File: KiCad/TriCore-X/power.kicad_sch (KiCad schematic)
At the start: 13 parts, among them U3 TPS56637RPAR

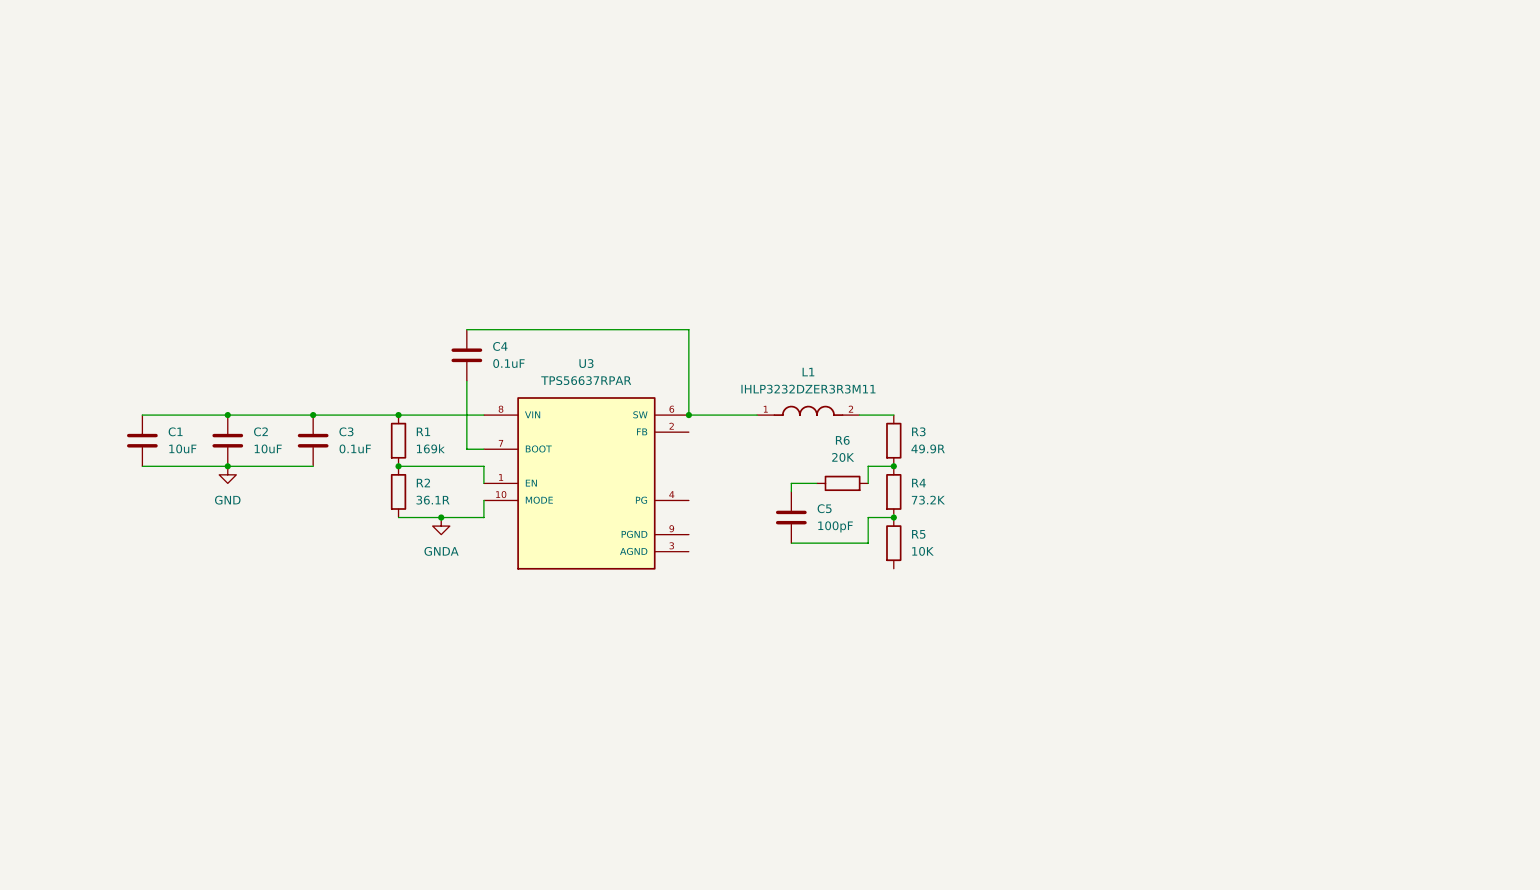
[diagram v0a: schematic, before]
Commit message: feat: design 5V and 12V power rails (schematic & PCB)
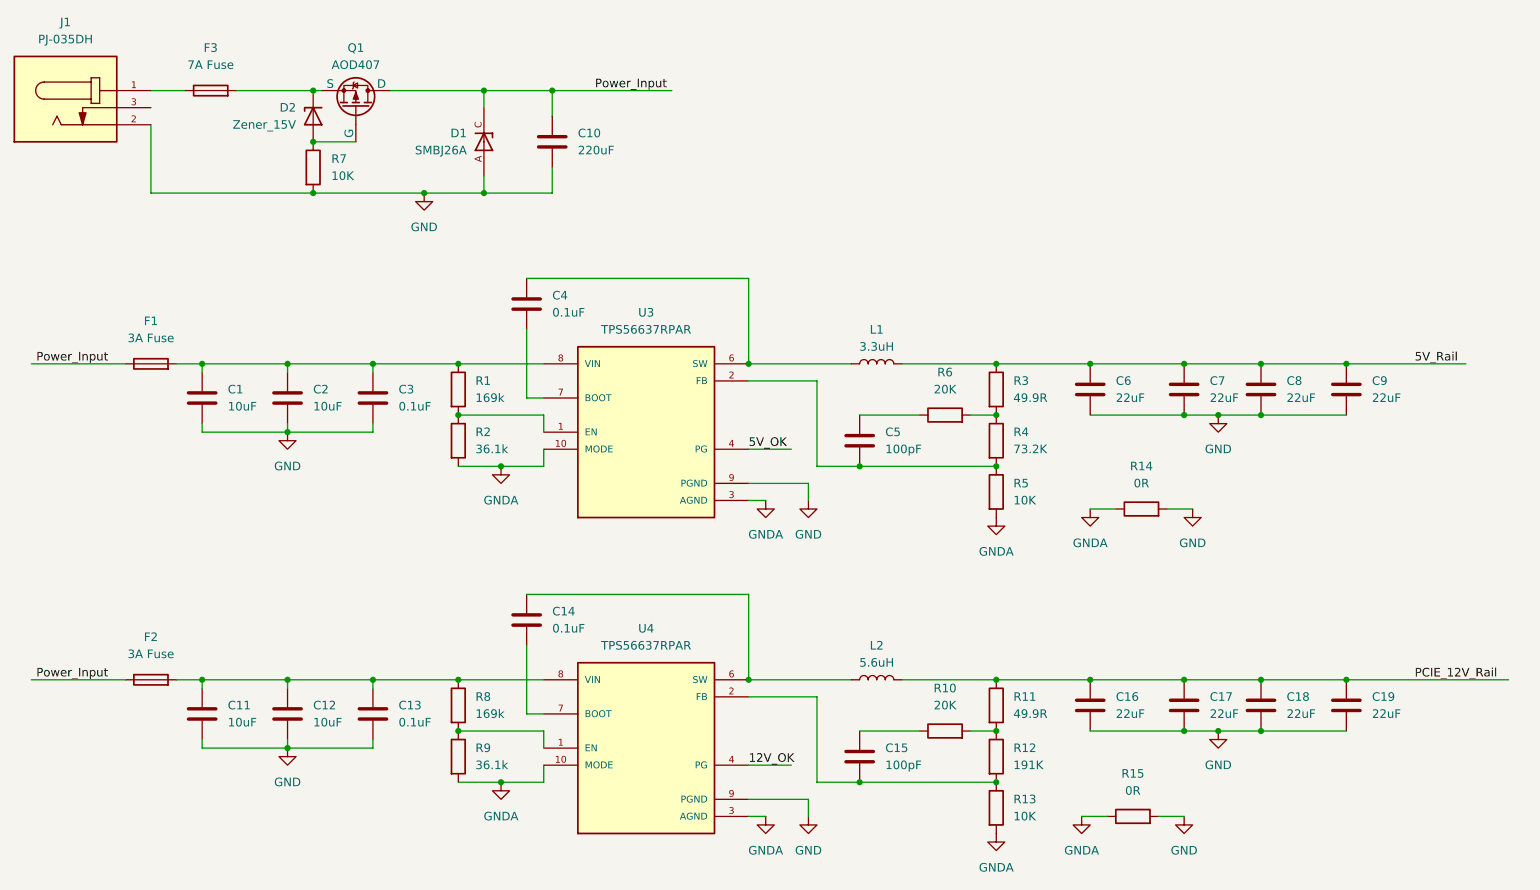
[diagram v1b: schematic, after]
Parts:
- removed L1: IHLP3232DZER3R3M11, IHLP3232DZER3R3M11:INDM8681X400N, symbol IHLP3232DZER3R3M11:IHLP3232DZER3R3M11
- added C10: 220uF, Capacitor_SMD:C_Elec_8x10.2, symbol Device:C
- added C11, C12: 10uF, Capacitor_SMD:C_0402_1005Metric, symbol Device:C
- added C13, C14: 0.1uF, Capacitor_SMD:C_0402_1005Metric, symbol Device:C
- added C15: 100pF, Capacitor_SMD:C_0402_1005Metric, symbol Device:C
- added C16, C17, C18, C19, C6, C7, C8, C9: 22uF, Capacitor_SMD:C_0805_2012Metric, symbol Device:C
- added D1: SMBJ26A, SMBJ26A:DIOM4336X265N, symbol SMBJ26A:SMBJ26A
- added D2: Zener_15V, Diode_SMD:D_SOD-123, symbol Device:D_Zener
- added F1, F2: 3A Fuse, Fuse:Fuse_1206_3216Metric, symbol Device:Fuse
- added F3: 7A Fuse, Fuse:Fuse_1206_3216Metric, symbol Device:Fuse
- added J1: PJ-035DH, DC_INPUT:CUI_PJ-035DH, symbol DC_INPUT:PJ-035DH
- added L1: 3.3uH, Inductor_SMD:L_Bourns_SRP7028A_7.3x6.6mm, symbol Device:L
- added L2: 5.6uH, Inductor_SMD:L_Bourns_SRP7028A_7.3x6.6mm, symbol Device:L
- added Q1: AOD407, Package_TO_SOT_SMD:TO-252-2, symbol Simulation_SPICE:PMOS
- added R10: 20K, Resistor_SMD:R_0402_1005Metric, symbol Device:R
- added R11: 49.9R, Resistor_SMD:R_0402_1005Metric, symbol Device:R
- added R12: 191K, Resistor_SMD:R_0402_1005Metric, symbol Device:R
- added R13, R7: 10K, Resistor_SMD:R_0402_1005Metric, symbol Device:R
- added R14, R15: 0R, Resistor_SMD:R_0402_1005Metric, symbol Device:R
- added R8: 169k, Resistor_SMD:R_0402_1005Metric, symbol Device:R
- added R9: 36.1k, Resistor_SMD:R_0402_1005Metric, symbol Device:R
- added U4: TPS56637RPAR, TPS56637RPAR:CONV_TPS56637RPAR, symbol TPS56637RPAR:TPS56637RPAR
- R2: value 36.1R -> 36.1k
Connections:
- net GND: now also U3.9 (PGND), C10.2, C11.2, C12.2, C13.2, C16.2, C17.2, C18.2, C19.2, C6.2, C7.2, C8.2, C9.2, D1.A, J1.2, R14.2, R15.2, R7.2, U4.9 (PGND)
- net GNDA: now also R5.2, U3.3 (AGND), R13.2, R14.1, R15.1, R9.2, U4.10 (MODE), U4.3 (AGND)
- net 5V_Rail: now reaches R3.1
- net 5V_Rail: now also C6.1, C7.1, C8.1, C9.1, L1.2
- net at C1.1, C2.1, C3.1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: now also F1.2
- net at C4.1, U3.6 (SW): now also L1.1
- net at C5.2, R4.2, R5.1: now also U3.2 (FB)
- net 5V_OK: now reaches U3.4 (PG)
- new net: C11.1, C12.1, C13.1, F2.2, R8.1, U4.8 (VIN)
- new net: C15.1, R10.1
- new net: R10.2, R11.2, R12.1
- new net: C15.2, R12.2, R13.1, U4.2 (FB)
- new net: R8.2, R9.1, U4.1 (EN)
- new net: C14.1, L2.1, U4.6 (SW)
- new net: C14.2, U4.7 (BOOT)
- new net: D2.2 (A), Q1.2 (G), R7.1
- new net: F3.1, J1.1
- new net: D2.1 (K), F3.2, Q1.3 (S)
- new net 12V_OK: U4.4 (PG)
- new net PCIE_12V_Rail: C16.1, C17.1, C18.1, C19.1, L2.2, R11.1
- new net Power_Input: C10.1, D1.C, F1.1, F2.1, Q1.1 (D)
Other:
- moved on the sheet: C1, C2, C3, C4, C5, R1, R2, R3, R4, R5, R6, U3

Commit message: feat : add some Expansion Ports (work in progress)
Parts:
- added U5: RK809-5, RK809-5:QFN-68_L7.0-W7.0-P0.35-BL-EP5.5, symbol RK809-5:RK809-5
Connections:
- net GND: now also U5.69 (EP)
- net 5V_Rail renamed +5V
- net PCIE_12V_Rail renamed +12V

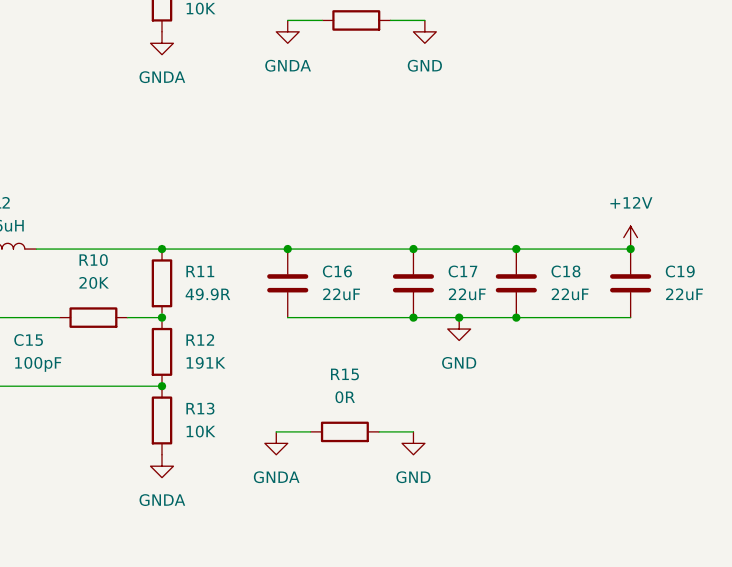
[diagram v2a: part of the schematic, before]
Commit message: refactor: change core MCU to STM32H723 and add LPDDR4/HDMI support
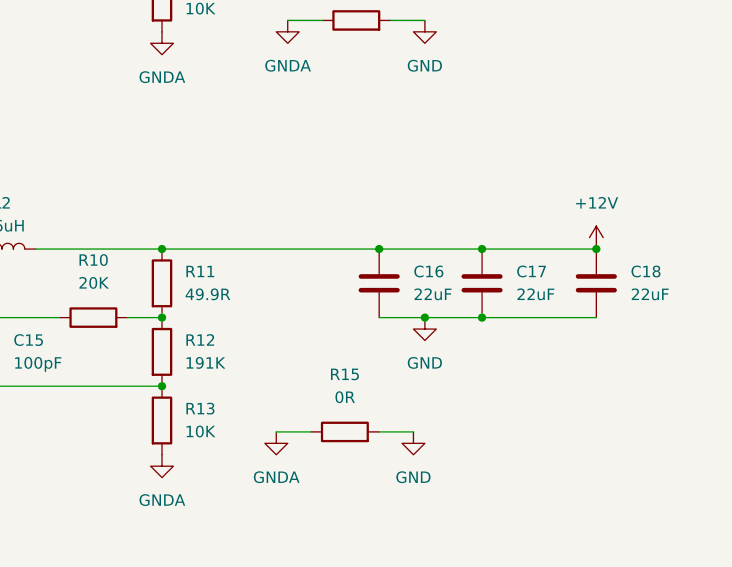
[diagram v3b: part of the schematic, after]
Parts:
- removed C16: 22uF, Capacitor_SMD:C_0805_2012Metric, symbol Device:C
- renumbered C17 to C16, C18 to C17, C19 to C18
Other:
- moved on the sheet: C16, C17, C18
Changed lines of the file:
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@@
 	)
 	(junction
-		(at 195.58 121.92)
+		(at 191.77 121.92)
 		(diameter 0)
 		(color 0 0 0 0)
@@
 	)
 	(junction
-		(at 176.53 114.3)
-		(diameter 0)
-		(color 0 0 0 0)
-	)
-	(junction
 		(at 125.73 114.3)
 		(diameter 0)
@@
 	)
 	(junction
-		(at 201.93 114.3)
+		(at 198.12 114.3)
 		(diameter 0)
 		(color 0 0 0 0)
@@
 	)
 	(junction
-		(at 214.63 114.3)
+		(at 210.82 114.3)
 		(diameter 0)
 		(color 0 0 0 0)
@@
 	)
 	(junction
-		(at 190.5 114.3)
+		(at 186.69 114.3)
 		(diameter 0)
 		(color 0 0 0 0)
@@
 	)
 	(junction
-		(at 190.5 121.92)
-		(diameter 0)
-		(color 0 0 0 0)
-	)
-	(junction
 		(at 57.15 67.31)
 		(diameter 0)
@@
 	)
 	(junction
-		(at 201.93 121.92)
+		(at 198.12 121.92)
 		(diameter 0)
 		(color 0 0 0 0)
@@
 	(wire
 		(pts
-			(xy 195.58 121.92) (xy 201.93 121.92)
-		)
-		(stroke
-			(width 0)
-			(type default)
-		)
-	)
-	(wire
-		(pts
-			(xy 176.53 121.92) (xy 190.5 121.92)
+			(xy 191.77 121.92) (xy 198.12 121.92)
 		)
 		(stroke
@@
 	(wire
 		(pts
-			(xy 190.5 114.3) (xy 201.93 114.3)
+			(xy 186.69 114.3) (xy 198.12 114.3)
 		)
 		(stroke
@@
 	(wire
 		(pts
-			(xy 201.93 121.92) (xy 214.63 121.92)
+			(xy 198.12 121.92) (xy 210.82 121.92)
 		)
 		(stroke
@@
 	(wire
 		(pts
-			(xy 162.56 114.3) (xy 176.53 114.3)
+			(xy 162.56 114.3) (xy 186.69 114.3)
 		)
 		(stroke
@@
 	(wire
 		(pts
-			(xy 176.53 114.3) (xy 190.5 114.3)
-		)
-		(stroke
-			(width 0)
-			(type default)
-		)
-	)
-	(wire
-		(pts
 			(xy 95.25 74.93) (xy 82.55 74.93)
 		)
@@
 	(wire
 		(pts
-			(xy 190.5 121.92) (xy 195.58 121.92)
+			(xy 186.69 121.92) (xy 191.77 121.92)
 		)
 		(stroke
@@
 	(wire
 		(pts
-			(xy 201.93 114.3) (xy 214.63 114.3)
+			(xy 198.12 114.3) (xy 210.82 114.3)
 		)
 		(stroke
@@
 	(symbol
 		(lib_id "Device:C")
-		(at 176.53 118.11 0)
-		(unit 1)
-		(exclude_from_sim no)
-		(in_bom yes)
-		(on_board yes)
-		(dnp no)
-		(fields_autoplaced yes)
-		(property "Reference" "C16"
-			(at 180.34 116.8399 0)
-			(effects
-				(font
-					(size 1.27 1.27)
-				)
-				(justify left)
-			)
-		)
-		(property "Value" "22uF"
-			(at 180.34 119.3799 0)
-			(effects
-				(font
-					(size 1.27 1.27)
-				)
-				(justify left)
-			)
-		)
-		(property "Footprint" "Capacitor_SMD:C_0805_2012Metric"
-			(at 177.4952 121.92 0)
-			(effects
-				(font
-					(size 1.27 1.27)
-				)
-				(hide yes)
-			)
-		)
-		(property "Datasheet" "~"
-			(at 176.53 118.11 0)
-			(effects
-				(font
-					(size 1.27 1.27)
-				)
-				(hide yes)
-			)
-		)
-		(property "Description" "Unpolarized capacitor"
-			(at 176.53 118.11 0)
-			(effects
-				(font
-					(size 1.27 1.27)
-				)
-				(hide yes)
-			)
-		)
-		(pin "2"
-		)
-		(pin "1"
-		)
-		(instances
-			(project "TriCore-X"
-				(path "/b9ed8ff9-3a91-4311-b656-324fcf6f7e0c/2a901d39-6beb-43c6-8602-9359e9e7f825"
-					(reference "C16")
-					(unit 1)
-				)
-			)
-		)
-	)
-	(symbol
-		(lib_id "Device:C")
 		(at 44.45 119.38 0)
 		(unit 1)
@@
 	(symbol
 		(lib_id "power:GND")
-		(at 195.58 121.92 0)
+		(at 191.77 121.92 0)
 		(unit 1)
 		(exclude_from_sim no)
@@
 		(fields_autoplaced yes)
 		(property "Reference" "#PWR028"
-			(at 195.58 128.27 0)
+			(at 191.77 128.27 0)
 			(effects
 				(font
@@
 		)
 		(property "Value" "GND"
-			(at 195.58 127 0)
+			(at 191.77 127 0)
 			(effects
 				(font
@@
 		)
 		(property "Footprint" ""
-			(at 195.58 121.92 0)
+			(at 191.77 121.92 0)
 			(effects
 				(font
@@
 		)
 		(property "Datasheet" ""
-			(at 195.58 121.92 0)
+			(at 191.77 121.92 0)
 			(effects
 				(font
@@
 		)
 		(property "Description" "Power symbol creates a global label with name \"GND\" , ground"
-			(at 195.58 121.92 0)
+			(at 191.77 121.92 0)
 			(effects
 				(font
@@
 	(symbol
 		(lib_id "Device:C")
-		(at 190.5 118.11 0)
+		(at 186.69 118.11 0)
 		(unit 1)
 		(exclude_from_sim no)
@@
 		(dnp no)
 		(fields_autoplaced yes)
-		(property "Reference" "C17"
-			(at 194.31 116.8399 0)
+		(property "Reference" "C16"
+			(at 190.5 116.8399 0)
 			(effects
 				(font
@@
 		)
 		(property "Value" "22uF"
-			(at 194.31 119.3799 0)
+			(at 190.5 119.3799 0)
 			(effects
 				(font
@@
 		)
 		(property "Footprint" "Capacitor_SMD:C_0805_2012Metric"
-			(at 191.4652 121.92 0)
+			(at 187.6552 121.92 0)
 			(effects
 				(font
@@
 		)
 		(property "Datasheet" "~"
-			(at 190.5 118.11 0)
+			(at 186.69 118.11 0)
 			(effects
 				(font
@@
 		)
 		(property "Description" "Unpolarized capacitor"
-			(at 190.5 118.11 0)
+			(at 186.69 118.11 0)
 			(effects
 				(font
@@
 			(project "TriCore-X"
 				(path "/b9ed8ff9-3a91-4311-b656-324fcf6f7e0c/2a901d39-6beb-43c6-8602-9359e9e7f825"
-					(reference "C17")
+					(reference "C16")
 					(unit 1)
 				)
@@
 	(symbol
 		(lib_id "Device:C")
-		(at 201.93 118.11 0)
+		(at 198.12 118.11 0)
 		(unit 1)
 		(exclude_from_sim no)
@@
 		(dnp no)
 		(fields_autoplaced yes)
-		(property "Reference" "C18"
-			(at 205.74 116.8399 0)
+		(property "Reference" "C17"
+			(at 201.93 116.8399 0)
 			(effects
 				(font
@@
 		)
 		(property "Value" "22uF"
-			(at 205.74 119.3799 0)
+			(at 201.93 119.3799 0)
 			(effects
 				(font
@@
 		)
 		(property "Footprint" "Capacitor_SMD:C_0805_2012Metric"
-			(at 202.8952 121.92 0)
+			(at 199.0852 121.92 0)
 			(effects
 				(font
@@
 		)
 		(property "Datasheet" "~"
-			(at 201.93 118.11 0)
+			(at 198.12 118.11 0)
 			(effects
 				(font
@@
 		)
 		(property "Description" "Unpolarized capacitor"
-			(at 201.93 118.11 0)
+			(at 198.12 118.11 0)
 			(effects
 				(font
@@
 			(project "TriCore-X"
 				(path "/b9ed8ff9-3a91-4311-b656-324fcf6f7e0c/2a901d39-6beb-43c6-8602-9359e9e7f825"
-					(reference "C18")
+					(reference "C17")
 					(unit 1)
 				)
@@
 	(symbol
 		(lib_id "Device:C")
-		(at 214.63 118.11 0)
+		(at 210.82 118.11 0)
 		(unit 1)
 		(exclude_from_sim no)
@@
 		(dnp no)
 		(fields_autoplaced yes)
-		(property "Reference" "C19"
-			(at 218.44 116.8399 0)
+		(property "Reference" "C18"
+			(at 214.63 116.8399 0)
 			(effects
 				(font
@@
 		)
 		(property "Value" "22uF"
-			(at 218.44 119.3799 0)
+			(at 214.63 119.3799 0)
 			(effects
 				(font
@@
 		)
 		(property "Footprint" "Capacitor_SMD:C_0805_2012Metric"
-			(at 215.5952 121.92 0)
+			(at 211.7852 121.92 0)
 			(effects
 				(font
@@
 		)
 		(property "Datasheet" "~"
-			(at 214.63 118.11 0)
+			(at 210.82 118.11 0)
 			(effects
 				(font
@@
 		)
 		(property "Description" "Unpolarized capacitor"
-			(at 214.63 118.11 0)
+			(at 210.82 118.11 0)
 			(effects
 				(font
@@
 			(project "TriCore-X"
 				(path "/b9ed8ff9-3a91-4311-b656-324fcf6f7e0c/2a901d39-6beb-43c6-8602-9359e9e7f825"
-					(reference "C19")
+					(reference "C18")
 					(unit 1)
 				)
@@
 	(symbol
 		(lib_id "power:+12V")
-		(at 214.63 114.3 0)
+		(at 210.82 114.3 0)
 		(unit 1)
 		(exclude_from_sim no)
@@
 		(fields_autoplaced yes)
 		(property "Reference" "#PWR030"
-			(at 214.63 118.11 0)
+			(at 210.82 118.11 0)
 			(effects
 				(font
@@
 		)
 		(property "Value" "+12V"
-			(at 214.63 109.22 0)
+			(at 210.82 109.22 0)
 			(effects
 				(font
@@
 		)
 		(property "Footprint" ""
-			(at 214.63 114.3 0)
+			(at 210.82 114.3 0)
 			(effects
 				(font
@@
 		)
 		(property "Datasheet" ""
-			(at 214.63 114.3 0)
+			(at 210.82 114.3 0)
 			(effects
 				(font
@@
 		)
 		(property "Description" "Power symbol creates a global label with name \"+12V\""
-			(at 214.63 114.3 0)
+			(at 210.82 114.3 0)
 			(effects
 				(font

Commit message: feat: complete schematic for RK809-5 PMIC peripheral circuits
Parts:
- added C21, C22, C23, C24, C25, C26, C27, C28, C29, C30, C31, C32, C33, C34, C35, C36, C37, C40, C41, C42, C43, C45: 1uF, Capacitor_SMD:C_0402_1005Metric, symbol Device:C
- added C38, C39: 2.2uF, Capacitor_SMD:C_0402_1005Metric, symbol Device:C
- added C44, C46, C47, C48, C49, C50: 10uF, Capacitor_SMD:C_0402_1005Metric, symbol Device:C
- added C51, C52, C53, C54, C55, C56, C57, C58, C59, C60: 22uF, Capacitor_SMD:C_0805_2012Metric, symbol Device:C
- added C61, C62, C63: 100nF, Capacitor_SMD:C_0402_1005Metric, symbol Device:C
- added L3, L4, L5, L6, L7: FNR6045SR47NT, L_6045:IND-SMD_L6.0-W6.0_FNR60XXS, symbol L_6045:FNR6045SR47NT
- added R18: 82K, Resistor_SMD:R_0402_1005Metric, symbol Device:R
- added R19: 120K, Resistor_SMD:R_0402_1005Metric, symbol Device:R
- added R20, R21: 4.7K, Resistor_SMD:R_0402_1005Metric, symbol Device:R
- added R22: 100K, Resistor_SMD:R_0402_1005Metric, symbol Device:R
- added R23: 22K, Resistor_SMD:R_0402_1005Metric, symbol Device:R
- added R24, R25, R26: 10K, Resistor_SMD:R_0402_1005Metric, symbol Device:R
- added Y1: 32.768KHZ, Crystal:Crystal_DS26_D2.0mm_L6.0mm_Vertical, symbol Device:Crystal
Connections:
- net +5V: now also U5.10 (VCC2), U5.11 (VCC1), U5.24 (VCC3), U5.33 (VCC_SPK_HP), U5.54 (VCC9), U5.66 (VCC4), C44.1, C46.1, C47.1, C48.1, C49.1, C50.1, R22.1
- net GND: now also U5.14 (LRCLK), U5.15 (BCLK), U5.16 (MCLK), U5.17 (SDI), U5.19 (PDMCLK), U5.40 (HP_SNS), U5.47 (GNDREF), U5.56 (BATDIV), U5.62 (SNSP), U5.63 (SNSN), C21.2, C22.2, C23.2, C24.2, C25.2, C26.2, C27.2, C28.2, C29.2, C30.2, C31.2, C32.2, C33.2, C34.2, C35.2, C36.2, C37.2, C39.2, C40.2, C41.2, C42.2, C43.2, C44.2, C45.2, C46.2, C47.2, C48.2, C49.2, C50.2, C51.1, C52.1, C53.2, C54.2, C55.1, C56.2, C57.2, C58.1, C59.1, C60.2, C61.2, C63.2, R19.1, R23.2
- net RK809-5_SDA: now reaches U5.1 (SCL)
- net RK809-5_SDA: now also R21.2
- net at U5.12 (SW1): now also L5.1
- net BUCK1: now reaches U5.13 (FB1)
- net BUCK1: now also C52.2, C60.1, L5.2
- net RK809-5_SCL: now reaches U5.2 (SDA)
- net RK809-5_SCL: now also R20.2
- net VLDO3: now reaches U5.20 (LDO3)
- net VLDO3: now also C26.1
- net VLDO2: now reaches U5.21 (LDO2)
- net VLDO2: now also C25.1
- net VCC SYS: now reaches U5.22 (VCC5)
- net VCC SYS: now also C23.1
- net VLDOI: now reaches U5.23 (LDO1)
- net VLDOI: now also C24.1
- net at U5.25 (SW3): now also L7.1
- net BUCK3: now reaches U5.26 (VBUCK3)
- net BUCK3: now also C55.2, C57.1, L7.2, R18.2
- net at U5.27 (FB3): now also R18.1, R19.2
- net VLDO4: now reaches U5.28 (LDO4)
- net VLDO4: now also C28.1
- net VLDO5: now reaches U5.29 (LDO5)
- net VLDO5: now also C29.1
- net VLDO7: now reaches U5.3 (LDO7)
- net VLDO7: now also C32.1
- net BUCK 5: now reaches U5.30 (VCC6)
- net BUCK 5: now also C27.1
- net VLDO6: now reaches U5.31 (LDO6)
- net VLDO6: now also C30.1
- net at U5.35 (VCC_CPVSS): now also C39.1
- net at U5.36 (CPN): now also C38.1
- net at U5.37 (CPP): now also C38.2
- net at U5.38 (VCC_CPVDD): now also C40.1
- net BUCK5: now reaches U5.4 (VCC7)
- net BUCK5: now also U5.57 (VCC8), U5.59 (FB5), C22.1, C31.1, C54.1, C59.2, L3.2
- net at U5.44 (VCC_1P8A): now also C41.1
- net VCC_RTC: now reaches U5.45 (VCC_RTC)
- net VCC_RTC: now also C43.1
- net at U5.46 (VREF): now also C35.1
- net at U5.48 (VCC_1P8D): now also C42.1
- net VLDO8: now reaches U5.5 (LDO8)
- net VLDO8: now also C33.1
- net at U5.50 (XIN): now also C37.1, Y1.2
- net at U5.51 (XOUT): now also C36.1, Y1.1
- net at U5.53 (SW5): now also L3.1
- net VSWOUTI: now reaches U5.55 (SWOUT1)
- net VSWOUTI: now also C45.1
- net VSWOUT2: now reaches U5.58 (SWOUT2)
- net VSWOUT2: now also C21.1
- net VLDO9: now reaches U5.6 (LDO9)
- net VLDO9: now also C34.1
- net at U5.61 (VDC): now also C61.1, R22.2, R23.1
- net BUCK4: now reaches U5.64 (FB4)
- net BUCK4: now also C53.1, C58.2, L4.2, R20.1, R21.1, R24.1, R25.2, R26.2
- net at U5.65 (SW4): now also L4.1
- net at U5.67 (RESETB): now also C63.1, R26.1
- net at U5.68 (CLK32K): now also R25.1
- net at U5.7 (INT): now also R24.2
- net BUCK2: now reaches U5.8 (FB2)
- net BUCK2: now also C51.2, C56.1, L6.2
- net at U5.9 (SW2): now also L6.1
- no-connect marks 0 -> 7
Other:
- moved on the sheet: U5
